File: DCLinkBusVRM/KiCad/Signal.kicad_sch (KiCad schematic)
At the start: 60 parts, among them IC4 LM358DR, IC5 LM358DR, IC6 MCP2515-e_ST, IC7 TJA1050T_CM,118, SW1 SW_Push, U2 TL431AIDBZR, U4 TMP36xS, U5 TMP36xS, Y1 8MHz

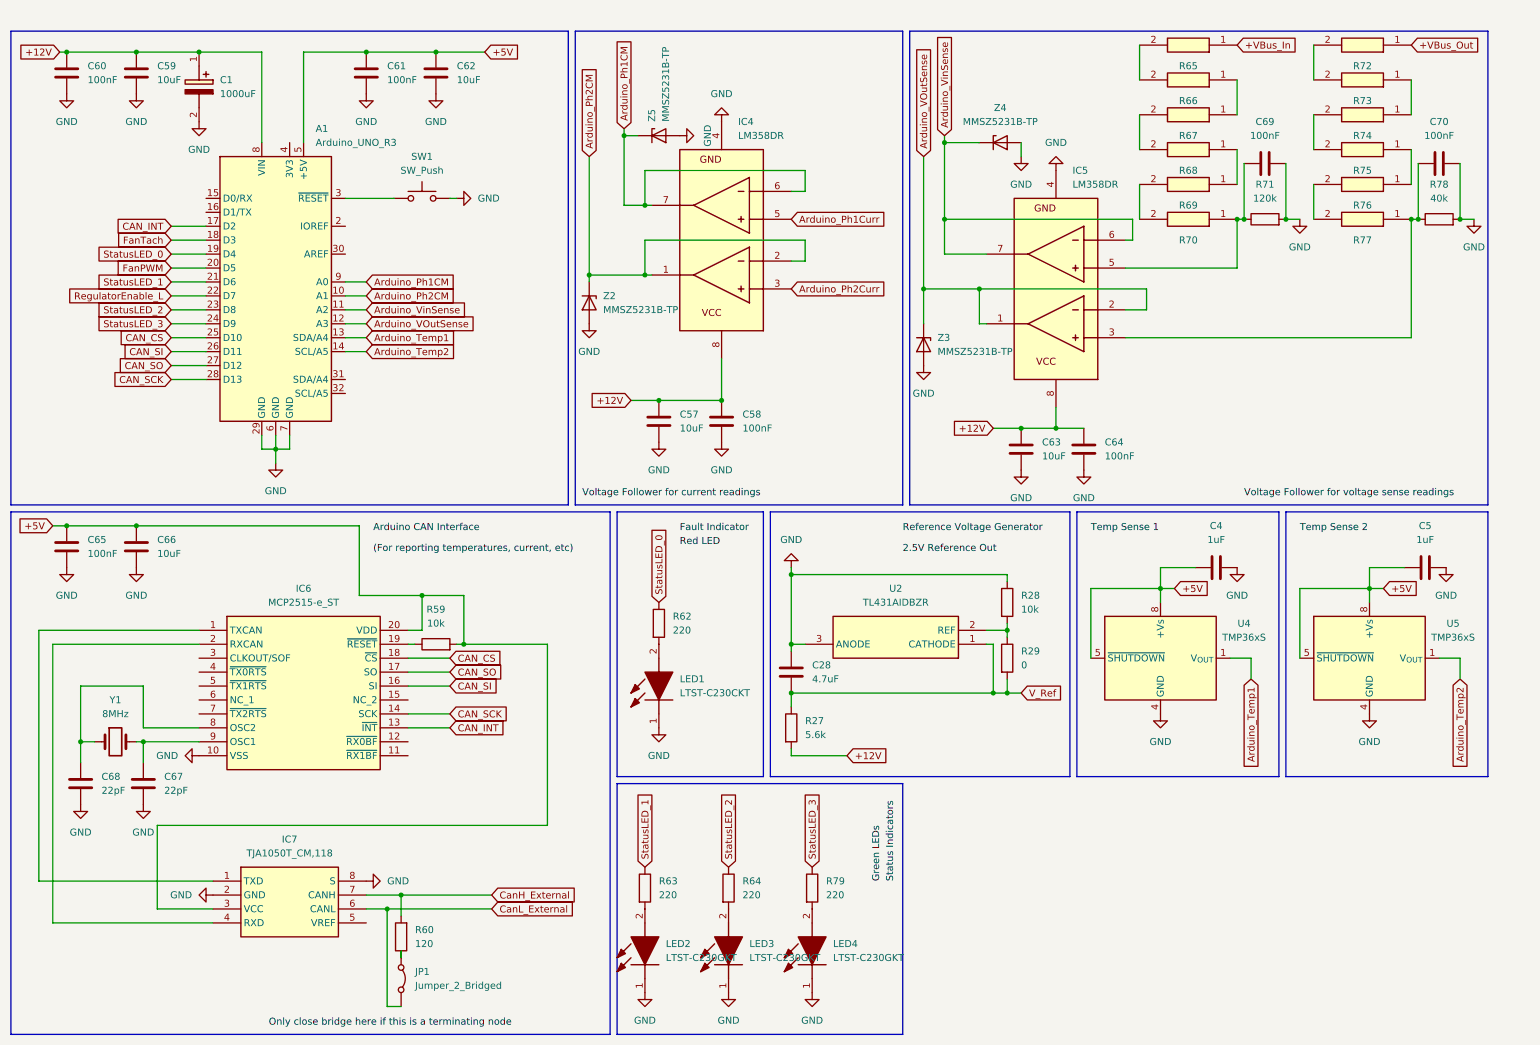
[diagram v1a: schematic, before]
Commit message: Update Canbus protocol for vrm
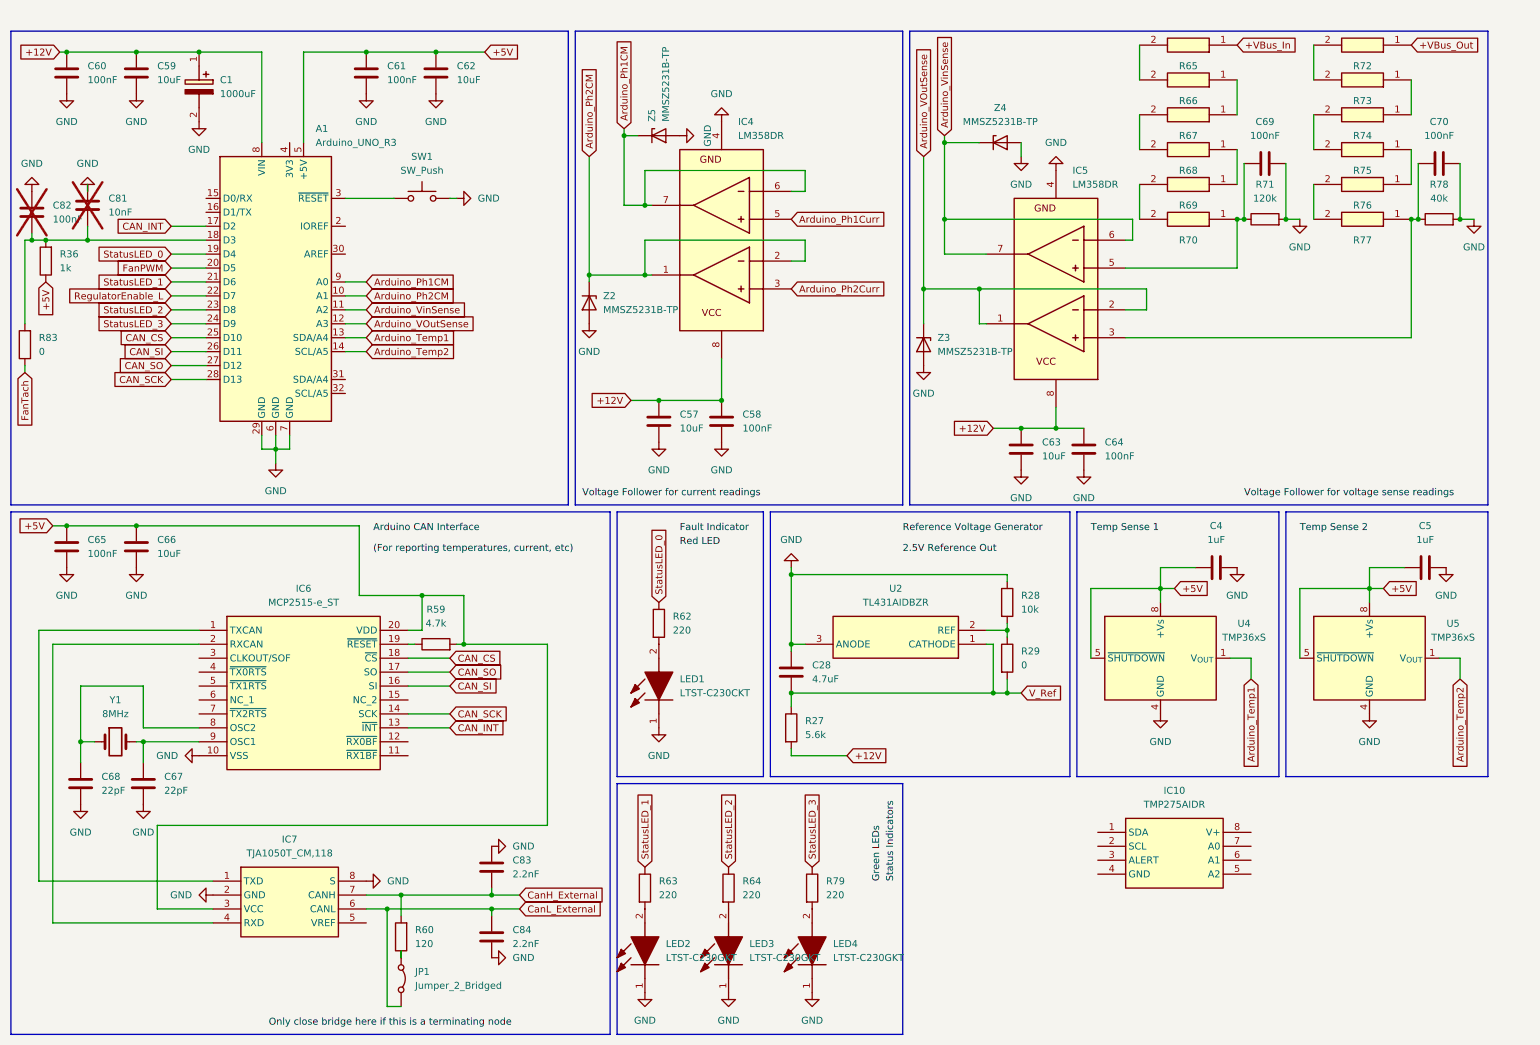
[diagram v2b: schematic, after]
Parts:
- added C81: 10nF, Capacitor_SMD:C_1210_3225Metric_Pad1.33x2.70mm_HandSolder, symbol Device:C
- added C82: 100nF, Capacitor_SMD:C_1210_3225Metric_Pad1.33x2.70mm_HandSolder, symbol Device:C
- added C83, C84: 2.2nF, Capacitor_SMD:C_1210_3225Metric_Pad1.33x2.70mm_HandSolder, symbol Device:C
- added IC10: TMP275AIDR, SOIC127P600X175-8N, symbol InverterCom:TMP275AIDR
- added R36: 1k, Resistor_SMD:R_1210_3225Metric_Pad1.30x2.65mm_HandSolder, symbol Device:R
- added R83: 0, Resistor_SMD:R_1210_3225Metric_Pad1.30x2.65mm_HandSolder, symbol Device:R
- R59: value 10k -> 4.7k
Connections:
- net +5V: now also R36.1
- net CanH_External: now also C83.2
- net CanL_External: now also C84.1
- net FanTach: now also R83.1; no longer A1.18 (D3)
- net GND: now also C81.1, C82.1, C83.1, C84.2
- new net: A1.18 (D3), C81.2, C82.2, R36.2, R83.2
